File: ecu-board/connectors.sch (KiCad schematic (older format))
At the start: 4 parts

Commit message: Schematic completed. Now to confirm details and proof-read.
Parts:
- removed J?: Crankshaft Hall connector, symbol Connector:Conn_01x04_Female
- removed J?: Camshaft Hall connector, symbol Connector:Conn_01x04_Female
- removed J?: Wheel Hall connector, symbol Connector:Conn_01x04_Female
- removed J?: MAP connector, symbol Connector:Conn_01x03_Female
- added D1: D, symbol Device:D
- added F2, F3: 30A Fuse, symbol Device:Fuse_Small
- added F4, F5: 5A Fuse, symbol Device:Fuse_Small
- added J10: Injector connector, symbol Connector:Screw_Terminal_01x02
- added J11: MAP connector, symbol Connector:Screw_Terminal_01x03
- added J12, J15: EGO connector, symbol Connector:Screw_Terminal_01x03
- added J13: Chrankshaft Hall connector, symbol Connector:Screw_Terminal_01x04
- added J14: Camshaft Hall connector, symbol Connector:Screw_Terminal_01x04
- added J2: Battery power conenctor, symbol Connector:Screw_Terminal_01x02
- added J3: Button input connector, symbol Connector:Screw_Terminal_01x03
- added J4: Motor conenctor, symbol Connector:Screw_Terminal_01x02
- added J5: Serial DB9 connector, symbol Connector:DB9_Female
- added J6: Ignition 1 connector, symbol Connector:Screw_Terminal_01x02
- added J7: Ignition 2 connector, symbol Connector:Screw_Terminal_01x02
- added J8: IAT connector, symbol Connector:Screw_Terminal_01x02
- added J9: CLT connector, symbol Connector:Screw_Terminal_01x02
- added R2, R3: 10k, symbol Device:R
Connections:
- net labels added: +BATT, GNDPWR, clt_signal, ego_signal, iat_signal, ignition1_input, ignition2_input, injector_input, main_power_signal, serial_GND, serial_rx, serial_tx, start_motor_power, start_motor_signal, tachometer_input
- net labels removed: wheel_sensor
- wire segments 26 -> 78
- no-connect marks 0 -> 6
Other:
- note added: "Battery power is only connected to the main power \nrelay, as well as the normally open bistable power \nswitch controlling said relay."
- note added: "Battery\n\n"
- note added: "Button input\n"
- note added: "Button inputs for relay control of main power and \nstarter motor."
- note added: "Connection to the Raspbery Pi based HMI.\n"
- note added: "DB9 serial connector for mapping of MicroSquirt.\n"
- note added: "EGO Lambda sensor"
- note added: "Hall Sensor Model: Littlefuse 55110-3M-03-A\nCrankshaft Sensor: xxxxx\nPinout:\n1. 3.8-24V\n2. Signal\n3. Shield\n4. GND"
- note added: "Hall sensors\n"
- note added: "Human Machine-Interface"
- note added: "Ignition"
- note added: "Injector input is switched by a \nnormally open dead mans switch."
- note added: "Injector\n"
- note added: "Intake Air Temperature\n"
- note added: "MAP sensor"
- note added: "Motor Coolant Temperature\n"
- note added: "RS232 Serial Port"
- note added: "Start motor\n"
- note added: "The electrical system is designed to function with \neither one or two ignition coils. Currently it is not \nyet decided how the final implementation will be."
- note added: "The start motor power is switched by a normally open \nmonostable switch."
- note removed: "Hall Sensor Model: Littlefuse 55110-3M-03-A\nCrankshaft Sensor Model: xxxxx\nPinout:\n1. 3.8-24V\n2. Signal\n3. Shield\n4. GND"
- note removed: "Hall Sensors\n"
- note removed: "MAP Sensor"

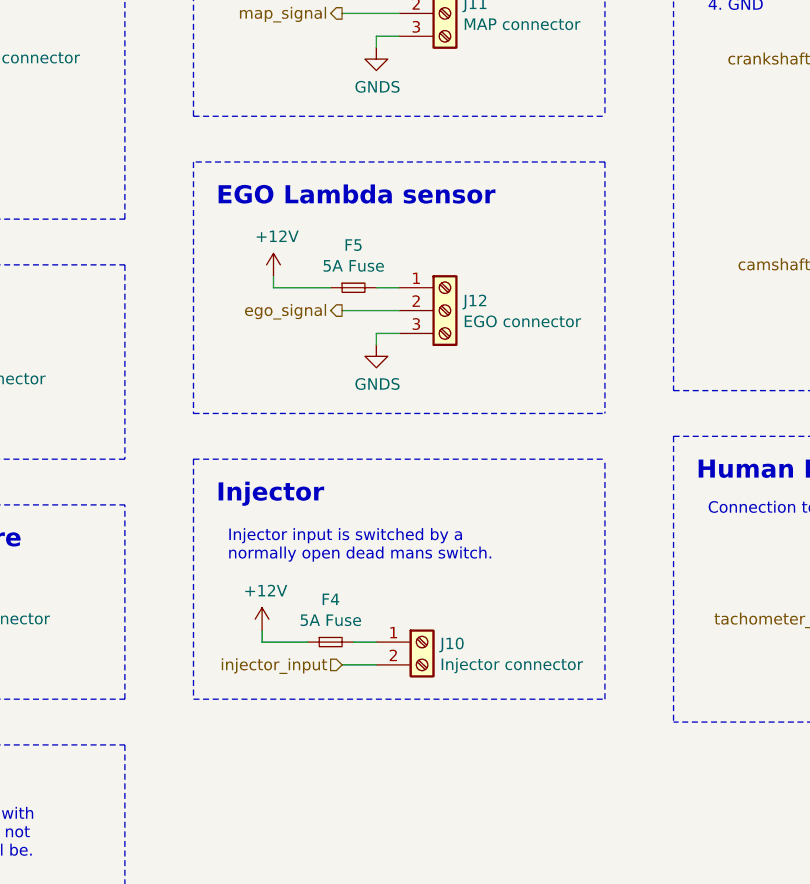
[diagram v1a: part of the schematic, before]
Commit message: Add Power Ground to lambda connector
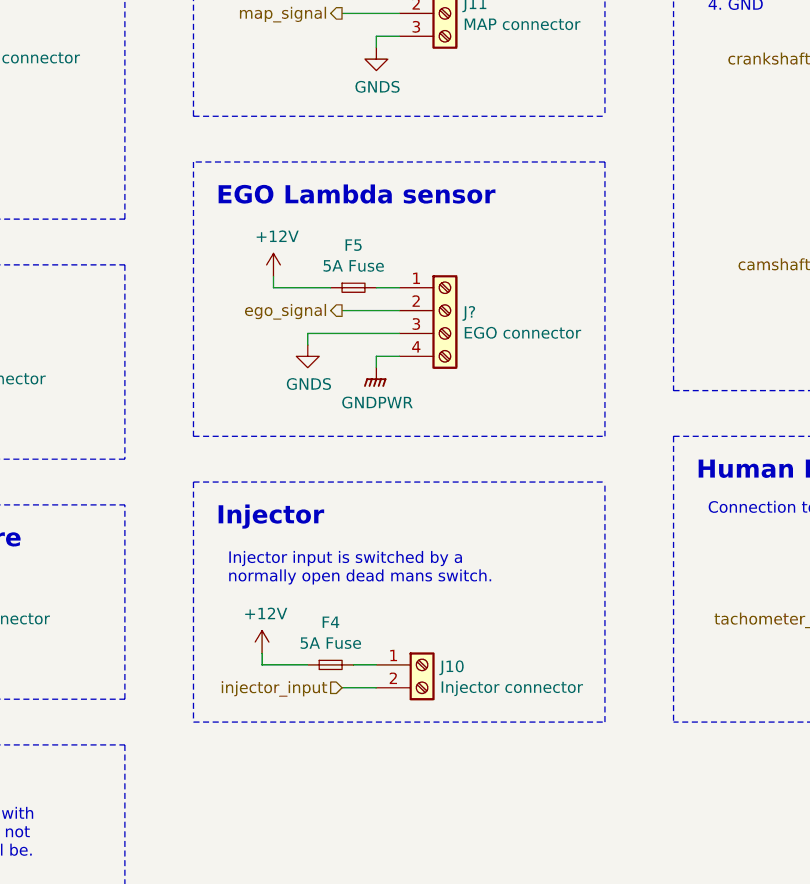
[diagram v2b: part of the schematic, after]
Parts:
- removed J12: EGO connector, symbol Connector:Screw_Terminal_01x03
- added J?: EGO connector, symbol Connector:Screw_Terminal_01x04
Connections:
- net GNDPWR: now also J?.4 (Pin_4)
- net GNDS: now also J?.3 (Pin_3)
- net ego_signal: now also J?.2 (Pin_2)
- net at F5.2: now also J?.1 (Pin_1)
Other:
- moved on the sheet: F4, J10

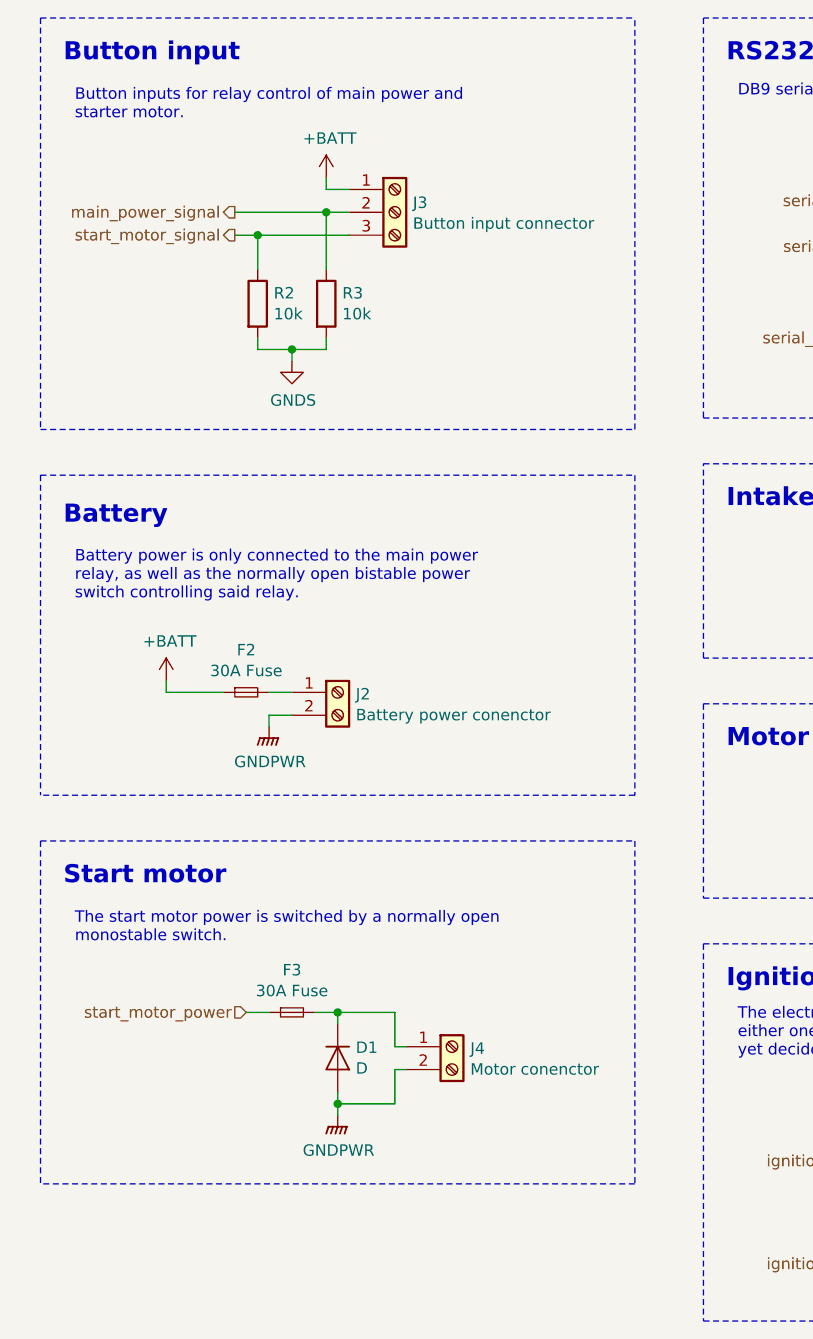
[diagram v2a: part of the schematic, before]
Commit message: Remove relay pull downs.
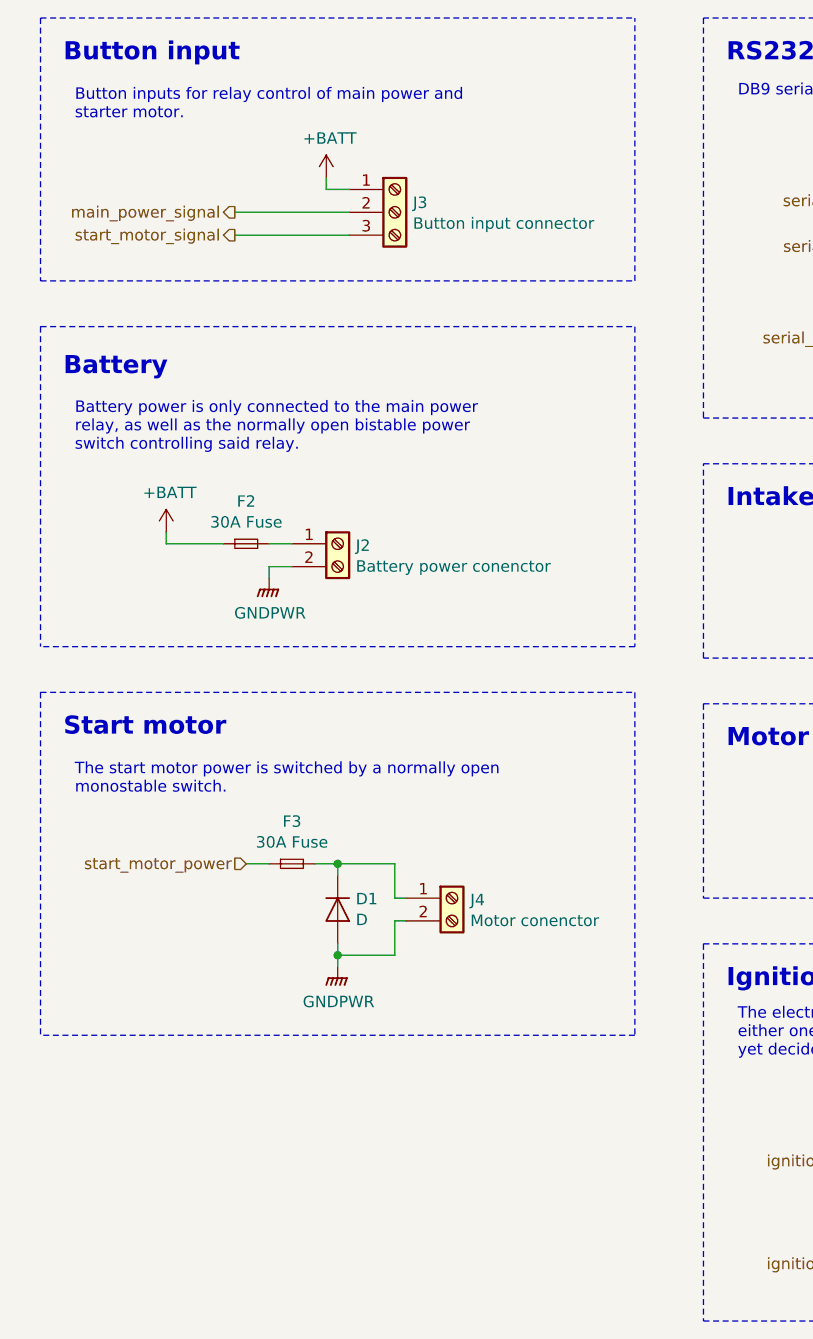
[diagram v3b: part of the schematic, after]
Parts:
- removed R2, R3: 10k, symbol Device:R
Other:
- moved on the sheet: D1, F2, F3, J2, J4
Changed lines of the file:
@@
 main_power_signal
-$Comp
-L Device:R R2
-U 1 1 5C59DE08
-P 1750 2150
-F 0 "R2" H 1820 2196 50  0000 L CNN
-F 1 "10k" H 1820 2105 50  0000 L CNN
-F 2 "" V 1680 2150 50  0001 C CNN
-F 3 "~" H 1750 2150 50  0001 C CNN
-F 4 "1700251" H 50  0   50  0001 C CNN "Farnell"
-	1    1750 2150
-	1    0    0    -1
-$EndComp
-$Comp
-L Device:R R3
-U 1 1 5C59DE98
-P 2050 2150
-F 0 "R3" H 2120 2196 50  0000 L CNN
-F 1 "10k" H 2120 2105 50  0000 L CNN
-F 2 "" V 1980 2150 50  0001 C CNN
-F 3 "~" H 2050 2150 50  0001 C CNN
-F 4 "1700251" H 50  0   50  0001 C CNN "Farnell"
-	1    2050 2150
-	1    0    0    -1
-$EndComp
-Wire Wire Line
-	2150 1750 2050 1750
-Wire Wire Line
-	1650 1850 1750 1850
-Wire Wire Line
-	2050 2000 2050 1750
-Connection ~ 2050 1750
-Wire Wire Line
-	2050 1750 1650 1750
-Wire Wire Line
-	1750 2000 1750 1850
-Connection ~ 1750 1850
-Wire Wire Line
-	1750 1850 2150 1850
-$Comp
-L power:GNDS #PWR08
-U 1 1 5C5A5599
-P 1900 2400
-F 0 "#PWR08" H 1900 2150 50  0001 C CNN
-F 1 "GNDS" H 1905 2227 50  0000 C CNN
-F 2 "" H 1900 2400 50  0001 C CNN
-F 3 "" H 1900 2400 50  0001 C CNN
-	1    1900 2400
-	1    0    0    -1
-$EndComp
-Wire Wire Line
-	2050 2300 2050 2350
-Wire Wire Line
-	2050 2350 1900 2350
-Wire Wire Line
-	1900 2350 1900 2400
-Wire Wire Line
-	1900 2350 1750 2350
-Wire Wire Line
-	1750 2350 1750 2300
-Connection ~ 1900 2350
-Wire Notes Line
-	800  900  800  2700
-Wire Notes Line
-	800  2700 3400 2700
-Wire Notes Line
-	3400 2700 3400 900
 $Comp
 L power:+BATT #PWR09
@@
 Wire Wire Line
 	2050 1650 2150 1650
-Text Notes 900  3250 0    79   ~ 16
+Text Notes 900  2600 0    79   ~ 16
 Battery\n\n
 Wire Notes Line
-	800  2900 3400 2900
+	800  2250 3400 2250
 $Comp
 L Device:Fuse_Small F5
@@
 L Connector:Screw_Terminal_01x02 J2
 U 1 1 5C5C3CF5
-P 2100 3850
-F 0 "J2" H 2179 3842 50  0000 L CNN
-F 1 "Battery power conenctor" H 2179 3751 50  0000 L CNN
-F 2 "" H 2100 3850 50  0001 C CNN
-F 3 "~" H 2100 3850 50  0001 C CNN
-F 4 "1716921, 2859411" H 2100 3850 50  0001 C CNN "Farnell"
-	1    2100 3850
-	1    0    0    -1
-$EndComp
-Text Notes 950  3450 0    50   ~ 0
+P 2100 3200
+F 0 "J2" H 2179 3192 50  0000 L CNN
+F 1 "Battery power conenctor" H 2179 3101 50  0000 L CNN
+F 2 "" H 2100 3200 50  0001 C CNN
+F 3 "~" H 2100 3200 50  0001 C CNN
+F 4 "1716921, 2859411" H 2100 3200 50  0001 C CNN "Farnell"
+	1    2100 3200
+	1    0    0    -1
+$EndComp
+Text Notes 950  2800 0    50   ~ 0
 Battery power is only connected to the main power \nrelay, as well as the normally open bistable power \nswitch controlling said relay.
 $Comp
 L power:+BATT #PWR06
 U 1 1 5C5D2F4D
-P 1350 3800
-F 0 "#PWR06" H 1350 3650 50  0001 C CNN
-F 1 "+BATT" H 1365 3973 50  0000 C CNN
-F 2 "" H 1350 3800 50  0001 C CNN
-F 3 "" H 1350 3800 50  0001 C CNN
-	1    1350 3800
-	1    0    0    -1
-$EndComp
-Wire Wire Line
-	1800 4000 1800 3950
-Wire Wire Line
-	1800 3950 1900 3950
+P 1350 3150
+F 0 "#PWR06" H 1350 3000 50  0001 C CNN
+F 1 "+BATT" H 1365 3323 50  0000 C CNN
+F 2 "" H 1350 3150 50  0001 C CNN
+F 3 "" H 1350 3150 50  0001 C CNN
+	1    1350 3150
+	1    0    0    -1
+$EndComp
+Wire Wire Line
+	1800 3350 1800 3300
+Wire Wire Line
+	1800 3300 1900 3300
 $Comp
 L Device:Fuse_Small F2
 U 1 1 5C5D4B6E
-P 1700 3850
-F 0 "F2" H 1700 4035 50  0000 C CNN
-F 1 "30A Fuse" H 1700 3944 50  0000 C CNN
-F 2 "" H 1700 3850 50  0001 C CNN
-F 3 "~" H 1700 3850 50  0001 C CNN
-F 4 "2292904" H -5100 -650 50  0001 C CNN "Farnell"
-	1    1700 3850
-	1    0    0    -1
-$EndComp
-Wire Wire Line
-	1900 3850 1800 3850
-Wire Wire Line
-	1350 3800 1350 3850
-Wire Wire Line
-	1350 3850 1600 3850
-Wire Notes Line
-	3400 4300 800  4300
-Wire Notes Line
-	800  2900 800  4300
-Wire Notes Line
-	3400 2900 3400 4300
-Text Notes 900  4700 0    79   ~ 16
+P 1700 3200
+F 0 "F2" H 1700 3385 50  0000 C CNN
+F 1 "30A Fuse" H 1700 3294 50  0000 C CNN
+F 2 "" H 1700 3200 50  0001 C CNN
+F 3 "~" H 1700 3200 50  0001 C CNN
+F 4 "2292904" H -5100 -1300 50  0001 C CNN "Farnell"
+	1    1700 3200
+	1    0    0    -1
+$EndComp
+Wire Wire Line
+	1900 3200 1800 3200
+Wire Wire Line
+	1350 3150 1350 3200
+Wire Wire Line
+	1350 3200 1600 3200
+Wire Notes Line
+	3400 3650 800  3650
+Wire Notes Line
+	800  2250 800  3650
+Wire Notes Line
+	3400 2250 3400 3650
+Text Notes 900  4050 0    79   ~ 16
 Start motor\n
 Wire Notes Line
-	800  4500 3400 4500
-Text Notes 950  4950 0    50   ~ 0
+	800  3850 3400 3850
+Text Notes 950  4300 0    50   ~ 0
 The start motor power is switched by a normally open \nmonostable switch.
 $Comp
 L Connector:Screw_Terminal_01x02 J4
 U 1 1 5C5E639D
-P 2600 5400
-F 0 "J4" H 2680 5392 50  0000 L CNN
-F 1 "Motor conenctor" H 2680 5301 50  0000 L CNN
-F 2 "" H 2600 5400 50  0001 C CNN
-F 3 "~" H 2600 5400 50  0001 C CNN
-F 4 "1716921, 2859411" H 2600 5400 50  0001 C CNN "Farnell"
-	1    2600 5400
+P 2600 4750
+F 0 "J4" H 2680 4742 50  0000 L CNN
+F 1 "Motor conenctor" H 2680 4651 50  0000 L CNN
+F 2 "" H 2600 4750 50  0001 C CNN
+F 3 "~" H 2600 4750 50  0001 C CNN
+F 4 "1716921, 2859411" H 2600 4750 50  0001 C CNN "Farnell"
+	1    2600 4750
 	1    0    0    -1
 $EndComp
@@
 L Device:Fuse_Small F3
 U 1 1 5C5E64A2
-P 1900 5250
-F 0 "F3" H 1900 5435 50  0000 C CNN
-F 1 "30A Fuse" H 1900 5344 50  0000 C CNN
-F 2 "" H 1900 5250 50  0001 C CNN
-F 3 "~" H 1900 5250 50  0001 C CNN
-F 4 "2292904" H -4900 750 50  0001 C CNN "Farnell"
-	1    1900 5250
+P 1900 4600
+F 0 "F3" H 1900 4785 50  0000 C CNN
+F 1 "30A Fuse" H 1900 4694 50  0000 C CNN
+F 2 "" H 1900 4600 50  0001 C CNN
+F 3 "~" H 1900 4600 50  0001 C CNN
+F 4 "2292904" H -4900 100 50  0001 C CNN "Farnell"
+	1    1900 4600
 	1    0    0    -1
 $EndComp
@@
 L power:GNDPWR #PWR07
 U 1 1 5C5EA433
-P 1800 4000
-F 0 "#PWR07" H 1800 3800 50  0001 C CNN
-F 1 "GNDPWR" H 1804 3846 50  0000 C CNN
-F 2 "" H 1800 3950 50  0001 C CNN
-F 3 "" H 1800 3950 50  0001 C CNN
-	1    1800 4000
+P 1800 3350
+F 0 "#PWR07" H 1800 3150 50  0001 C CNN
+F 1 "GNDPWR" H 1804 3196 50  0000 C CNN
+F 2 "" H 1800 3300 50  0001 C CNN
+F 3 "" H 1800 3300 50  0001 C CNN
+	1    1800 3350
 	1    0    0    -1
 $EndComp
@@
 L power:GNDPWR #PWR010
 U 1 1 5C5EA469
-P 2100 5700
-F 0 "#PWR010" H 2100 5500 50  0001 C CNN
-F 1 "GNDPWR" H 2104 5546 50  0000 C CNN
-F 2 "" H 2100 5650 50  0001 C CNN
-F 3 "" H 2100 5650 50  0001 C CNN
-	1    2100 5700
+P 2100 5050
+F 0 "#PWR010" H 2100 4850 50  0001 C CNN
+F 1 "GNDPWR" H 2104 4896 50  0000 C CNN
+F 2 "" H 2100 5000 50  0001 C CNN
+F 3 "" H 2100 5000 50  0001 C CNN
+	1    2100 5050
 	1    0    0    -1
 $EndComp
@@
 L Device:D D1
 U 1 1 5C5ECED0
-P 2100 5450
-F 0 "D1" V 2054 5529 50  0000 L CNN
-F 1 "D" V 2145 5529 50  0000 L CNN
-F 2 "" H 2100 5450 50  0001 C CNN
-F 3 "~" H 2100 5450 50  0001 C CNN
-	1    2100 5450
+P 2100 4800
+F 0 "D1" V 2054 4879 50  0000 L CNN
+F 1 "D" V 2145 4879 50  0000 L CNN
+F 2 "" H 2100 4800 50  0001 C CNN
+F 3 "~" H 2100 4800 50  0001 C CNN
+	1    2100 4800
 	0    1    1    0
 $EndComp
 Wire Wire Line
-	2400 5400 2350 5400
-Wire Wire Line
-	2400 5500 2350 5500
-Wire Wire Line
-	2100 5600 2100 5650
-Wire Wire Line
-	2100 5650 2350 5650
-Wire Wire Line
-	2350 5500 2350 5650
-Connection ~ 2100 5650
-Wire Wire Line
-	2100 5650 2100 5700
-Wire Wire Line
-	2350 5250 2100 5250
-Wire Wire Line
-	2100 5250 2100 5300
-Wire Wire Line
-	2350 5250 2350 5400
-Text HLabel 1700 5250 0    50   Input ~ 0
+	2400 4750 2350 4750
+Wire Wire Line
+	2400 4850 2350 4850
+Wire Wire Line
+	2100 4950 2100 5000
+Wire Wire Line
+	2100 5000 2350 5000
+Wire Wire Line
+	2350 4850 2350 5000
+Connection ~ 2100 5000
+Wire Wire Line
+	2100 5000 2100 5050
+Wire Wire Line
+	2350 4600 2100 4600
+Wire Wire Line
+	2100 4600 2100 4650
+Wire Wire Line
+	2350 4600 2350 4750
+Text HLabel 1700 4600 0    50   Input ~ 0
 start_motor_power
 Wire Wire Line
-	1700 5250 1800 5250
-Wire Wire Line
-	2000 5250 2100 5250
-Connection ~ 2100 5250
-Wire Notes Line
-	3400 6000 800  6000
-Wire Notes Line
-	800  4500 800  6000
-Wire Notes Line
-	3400 4500 3400 6000
+	1700 4600 1800 4600
+Wire Wire Line
+	2000 4600 2100 4600
+Connection ~ 2100 4600
+Wire Notes Line
+	3400 5350 800  5350
+Wire Notes Line
+	800  3850 800  5350
+Wire Notes Line
+	3400 3850 3400 5350
 Text Notes 3800 5150 0    79   ~ 16
 Ignition
@@
 Wire Wire Line
 	6750 3150 7150 3150
+Wire Wire Line
+	1650 1850 2150 1850
+Wire Wire Line
+	1650 1750 2150 1750
+Wire Notes Line
+	800  2050 3400 2050
+Wire Notes Line
+	3400 2050 3400 900
+Wire Notes Line
+	800  900  800  2050
 $EndSCHEMATC
